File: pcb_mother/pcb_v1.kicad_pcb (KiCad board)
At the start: 2 copper layers, 90.1 x 71.5 mm, 37 parts, among them J1 Conn_01x02, J10 Conn_01x02, J11 Conn_01x06, J12 Conn_01x02, J13 Conn_01x02, J14 Conn_01x06, J3 Conn_01x02, J4 Conn_01x02_Male, J5 Conn_01x02_Male, J6 Conn_01x02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

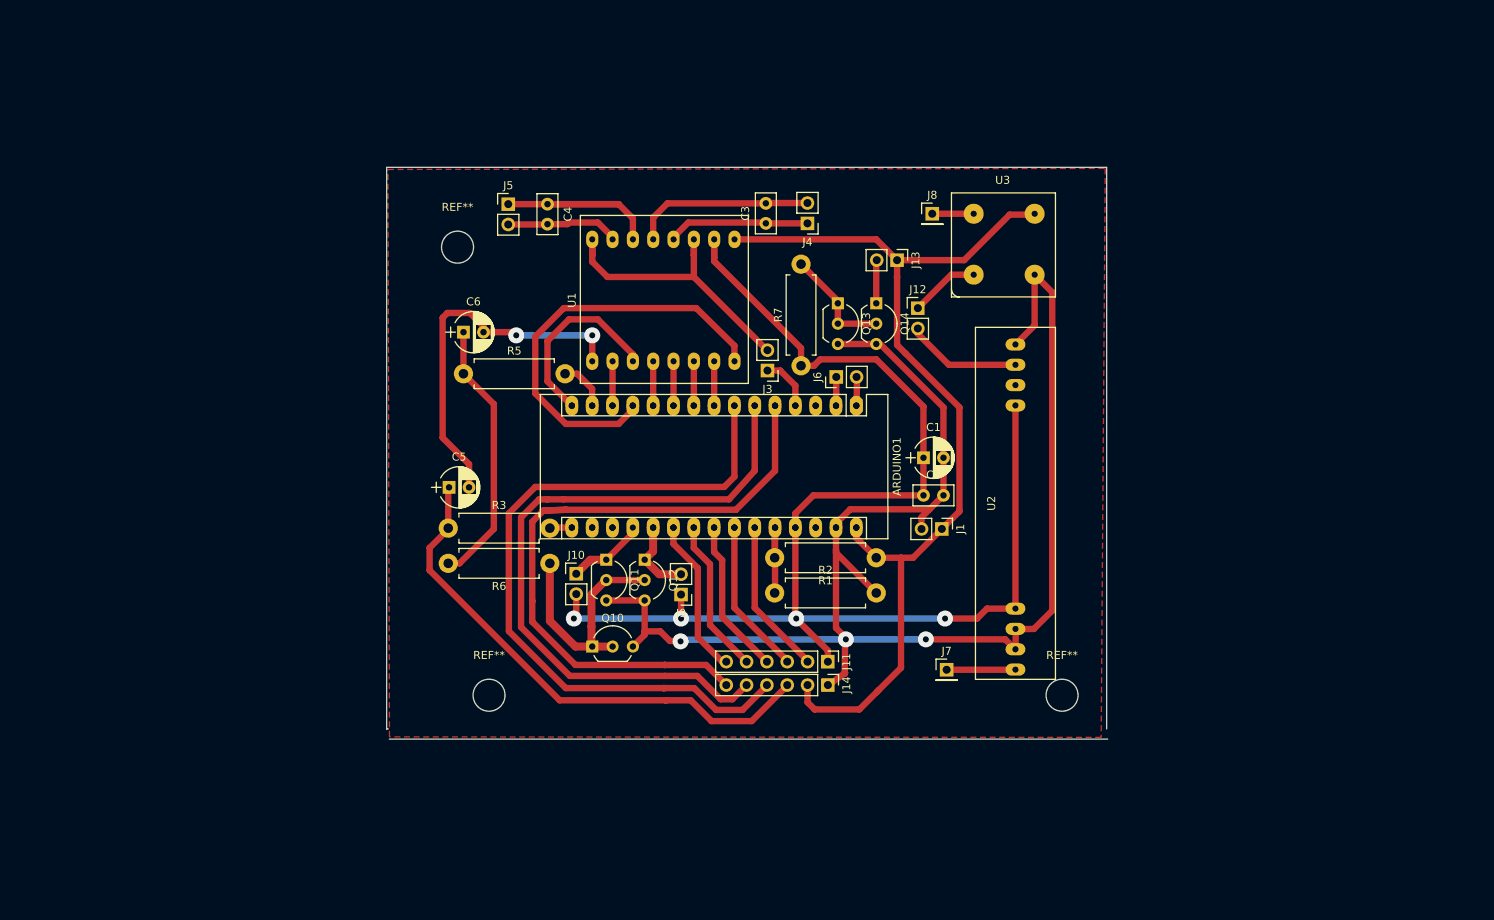
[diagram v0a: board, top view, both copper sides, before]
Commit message: Se moifico el esquematico y se esta acomodando para poder armar el pcb, la linea que se va a seguir es priorizar el funcionamiento antes que la estetica y el espacio.
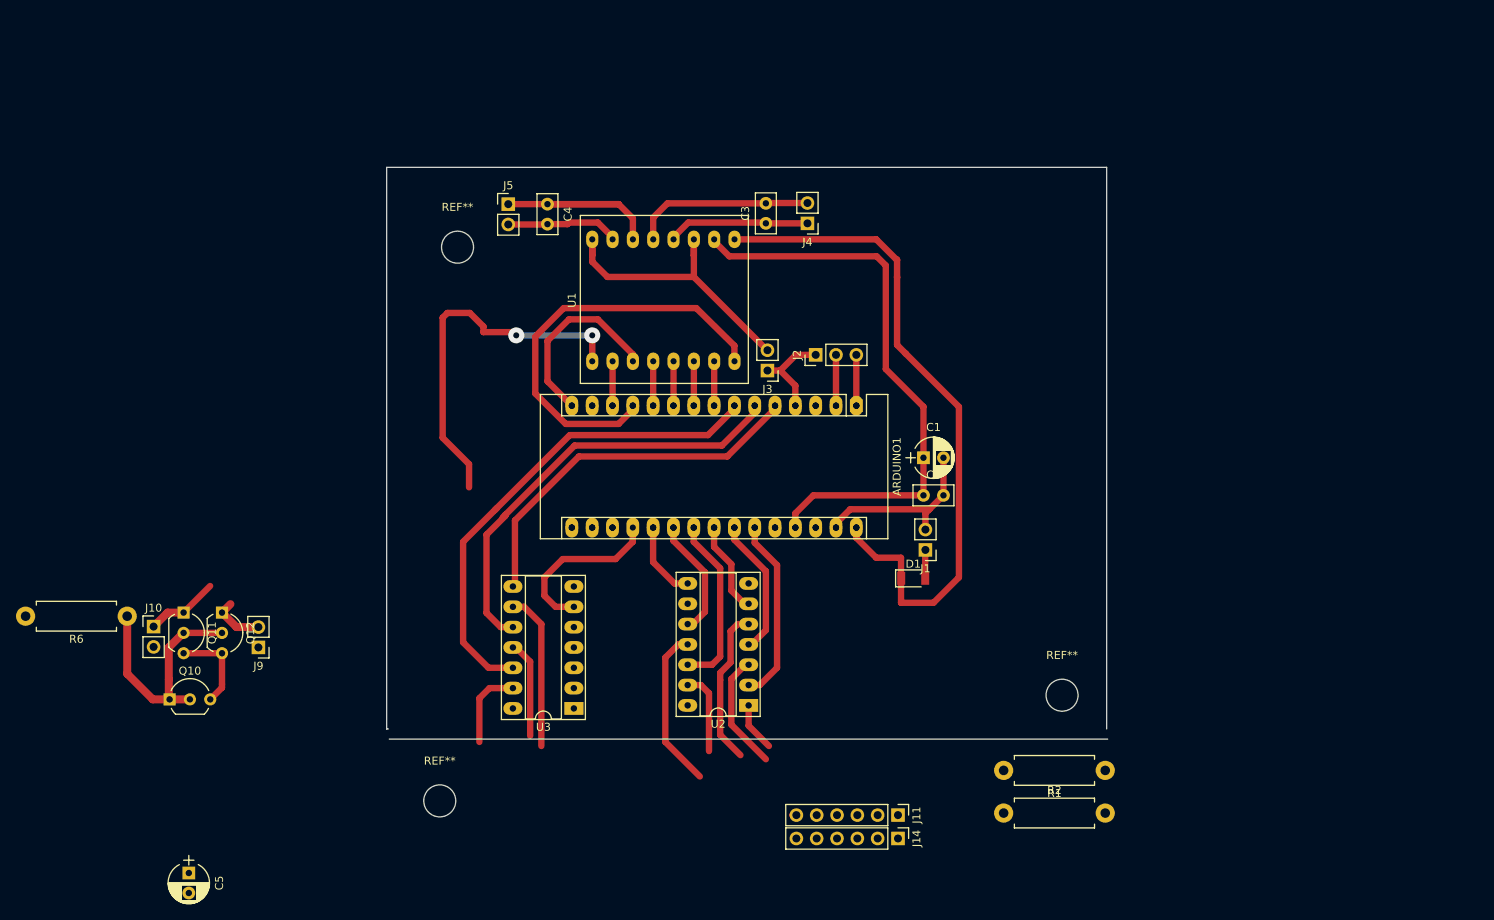
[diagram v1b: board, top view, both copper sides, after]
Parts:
- removed C6: 2.2u, Capacitors_THT:CP_Radial_D5.0mm_P2.50mm
- removed J12, J13, J6: Conn_01x02, Pin_Headers:Pin_Header_Straight_1x02_Pitch2.54mm
- removed J7, J8: Conn_01x01, Pin_Headers:Pin_Header_Straight_1x01_Pitch2.54mm
- removed Q13, Q14: 2N2219, TO_SOT_Packages_THT:TO-92_Inline_Wide
- removed R3, R5: 100k, Resistors_THT:R_Axial_DIN0411_L9.9mm_D3.6mm_P12.70mm_Horizontal
- removed R7: 220, Resistors_THT:R_Axial_DIN0411_L9.9mm_D3.6mm_P12.70mm_Horizontal
- added D1: D, Diodes_SMD:D_1206, F.Cu at (134.6, 103.4)
- added J2: Conn_01x03, Pin_Headers:Pin_Header_Straight_1x03_Pitch2.54mm, F.Cu at (122.4, 75.4)
- U2: value Rws433mhz -> 74HCT04; footprint Propias:rws433 -> Housings_DIP:DIP-14_W7.62mm_Socket_LongPads
- U3: value tws -> 74HCT04; footprint Propias:tws433 -> Housings_DIP:DIP-14_W7.62mm_Socket_LongPads
- moved U3 79.6 mm to (92.2, 119.6)
- moved C5 58.2 mm to (44.1, 140.2), turned to 270 degrees
- moved J10 53.2 mm to (39.7, 109.4)
- moved Q10 53.2 mm to (41.7, 118.5)
- moved Q11 53.2 mm to (43.4, 107.7)
- moved R6 53.2 mm to (36.4, 108.1)
- moved J9 53.2 mm to (52.8, 112.0)
- moved Q12 53.2 mm to (48.2, 107.7)
- moved U2 41.2 mm to (114.0, 119.3), turned to 180 degrees
- moved R2 39.7 mm to (145.9, 132.7)
- moved R1 39.1 mm to (158.6, 127.4)
- moved J11 21.1 mm to (132.7, 133.0)
- moved J14 21.1 mm to (132.7, 135.9)
- moved REF** 14.6 mm to (75.4, 131.2)
- moved J1 3.33 mm to (136.1, 99.8), turned to 180 degrees
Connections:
- ARDUINO1 pad 14: /Encoders -> Net-(ARDUINO1-Pad14)
- ARDUINO1 pad 16: /S_linea -> Net-(ARDUINO1-Pad16)
- ARDUINO1 pad 19: /E1 -> /A0_E1
- ARDUINO1 pad 20: /E2 -> /A1_E2
- ARDUINO1 pad 21: /L1_a -> /A2_l1_A
- ARDUINO1 pad 22: /L2_a -> /A3_l2_A
- ARDUINO1 pad 23: /L3_a -> /A4_l3_A
- ARDUINO1 pad 24: /L4_a -> /A5_l4_A
- ARDUINO1 pad 25: /L5_a -> /A6_l5_A
- ARDUINO1 pad 5: /L8_a -> /D2_L8_a
- ARDUINO1 pad 6: /L7_a -> /D3_L7_a
- ARDUINO1 pad 7: /L6_a -> /D4_L6_a
- C1 pad 1: /Vcc_5v -> Net-(C1-Pad1)
- J1 pad 1: /Vcc_bat -> Net-(D1-Pad2)
- R6 pad 2: Net-(C6-Pad1) -> /Vcc_5v
- U2 pad 1: /gnd_logic -> /L5_a
- U2 pad 2: /Comunicacion_RX -> /A6_l5_A
- U2 pad 3: Net-(U2-Pad3) -> /L4_a
- U2 pad 4: /Vcc_5v -> /A5_l4_A
- U2 pad 5: Net-(J7-Pad1) -> /L3_a
- U3 pad 1: /Comunicacion_TX -> (no net)
- U3 pad 2: /Vcc_bat -> (no net)
- U3 pad 3: /gnd_logic -> (no net)
- U3 pad 4: Net-(J8-Pad1) -> (no net)
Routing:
- net /gnd_logic: track 249.2 -> 93.4 mm, vias 5 -> 2
- net /Vcc_5v: track 175.8 -> 61.5 mm, vias 4 -> 0
- net /L6_a: track 91.8 -> 10.4 mm
- net /L7_a: track 86.4 -> 12.2 mm
- net /S_lin_ref_a: track 66.2 -> 0.06 mm
- net /L8_a: track 84.4 -> 19.8 mm
- net /D4_L6_a: track 0.00 -> 61.7 mm
- net /D3_L7_a: track 0.00 -> 55.1 mm
- net /D2_L8_a: track 0.00 -> 47.0 mm
- net /Vcc_bat: track 123.7 -> 86.8 mm
- net Net-(C6-Pad1): track 33.7 -> 0.00 mm
- net /A6_l5_A: track 0.00 -> 23.1 mm
- net /A0_E1: track 0.00 -> 23.1 mm
- net /A3_l2_A: track 0.00 -> 22.0 mm
- net /A5_l4_A: track 0.00 -> 17.5 mm
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- removed copper zone on F.Cu, net /gnd_logic

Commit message: modificacion del pcb previas a hacer una nueva rama.
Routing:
- net /E2: track 6.80 -> 30.5 mm

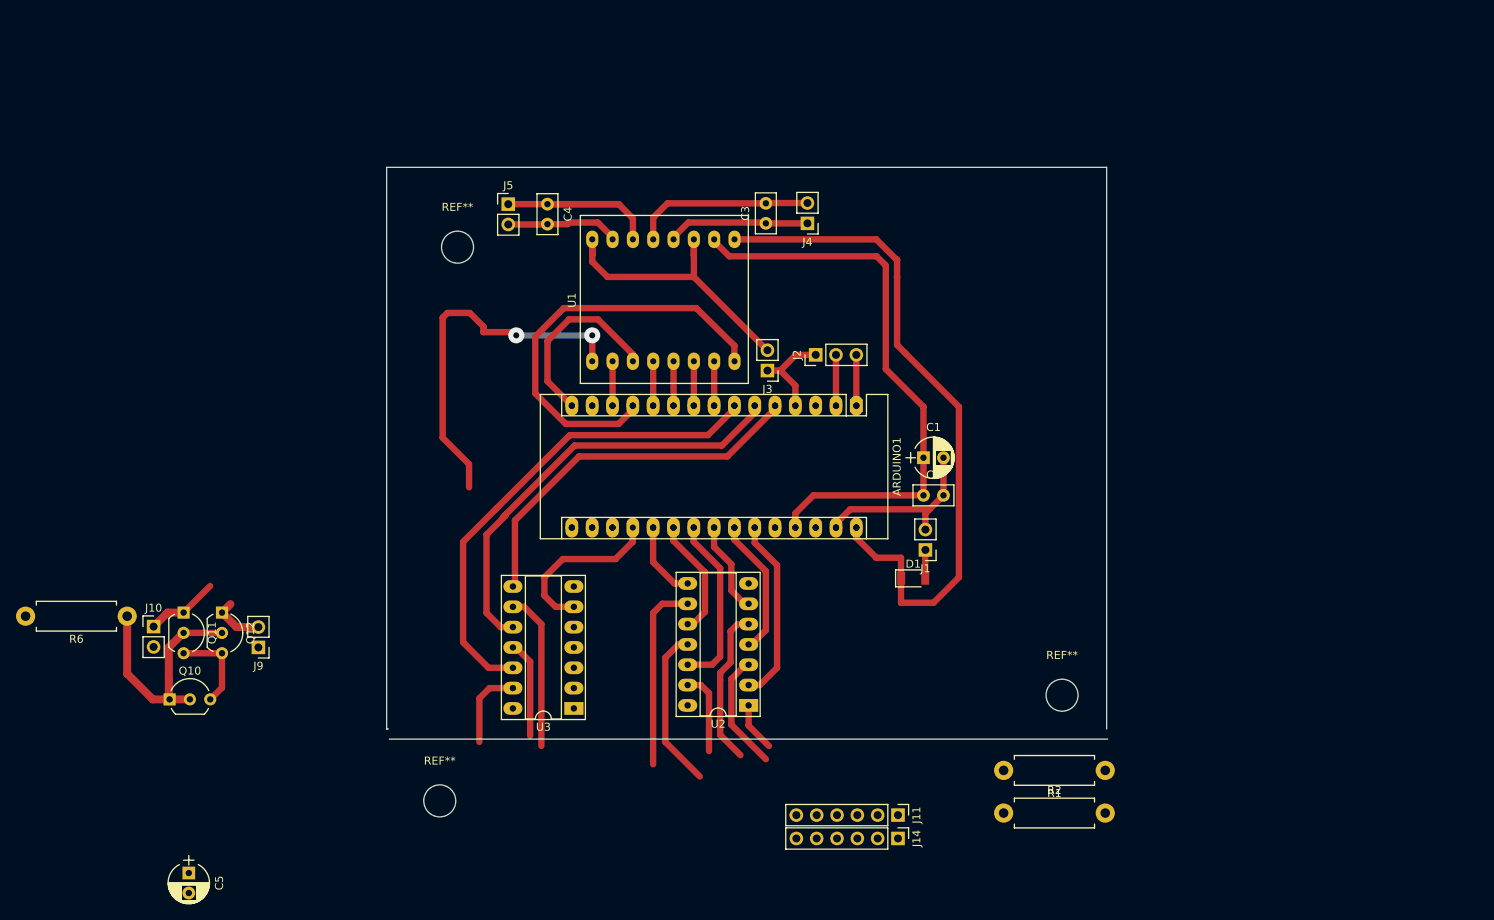
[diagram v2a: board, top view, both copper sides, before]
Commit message: Se pudiron acomodar los inversores, ahora falta poner el divisor resistivo, los planos de tierra, los puentes y los aujeros...
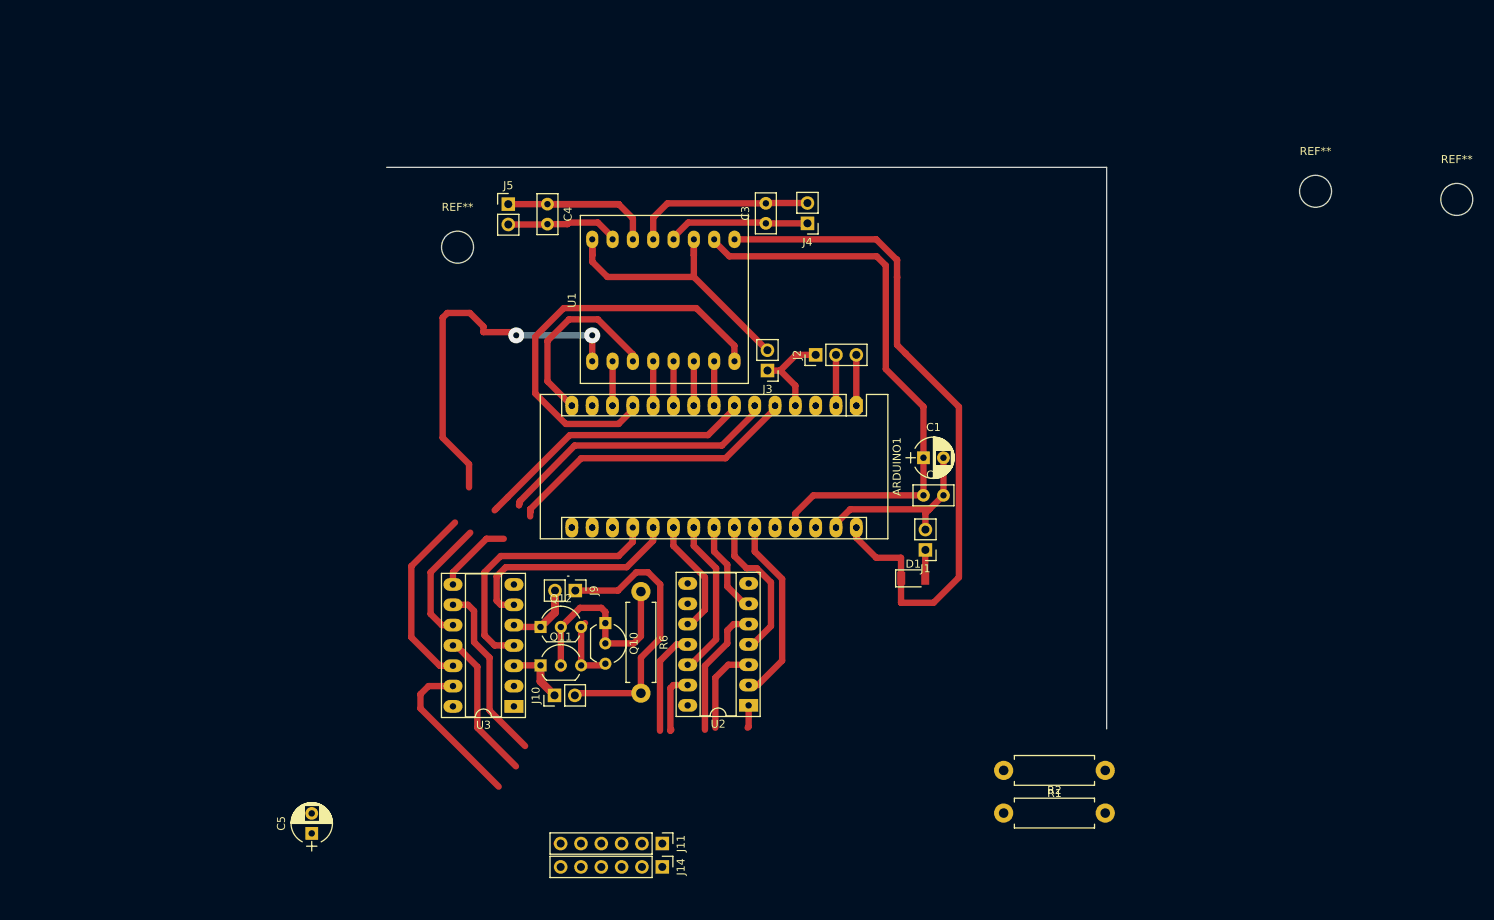
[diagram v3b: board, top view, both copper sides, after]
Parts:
- moved REF** 133.4 mm to (184.9, 55.0)
- moved REF** 79.2 mm to (202.6, 56.0)
- moved R6 64.3 mm to (100.6, 105.0), turned to 270 degrees
- moved Q10 55.3 mm to (96.1, 109.0), turned to 270 degrees
- moved J10 50.8 mm to (89.8, 118.0), turned to 90 degrees
- moved Q11 45.1 mm to (88.0, 114.3), turned to 0 degrees
- moved J9 40.2 mm to (92.4, 104.9), turned to 270 degrees
- moved Q12 39.9 mm to (88.0, 109.5), turned to 0 degrees
- moved J11 29.7 mm to (103.3, 136.5)
- moved J14 29.7 mm to (103.3, 139.4)
- moved C5 16.1 mm to (59.4, 135.3), turned to 90 degrees
- moved U3 7.50 mm to (84.7, 119.4)
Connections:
- ARDUINO1 pad 27: /Vcc_5v -> VCC
- C2 pad 1: /Vcc_5v -> VCC
- J10 pad 1: /E1 -> /E2
- J10 pad 2: /Vcc_5v -> VCC
- J11 pad 1: /Vcc_5v -> VCC
- J9 pad 1: /Vcc_5v -> VCC
- J9 pad 2: /E2 -> /E1
- Q11 pad 1: /E1 -> /E2
- Q12 pad 1: /E2 -> /E1
- R6 pad 2: /Vcc_5v -> VCC
- U1 pad 2: /Vcc_5v -> VCC
- U2 pad 8: /A1_E2 -> (no net)
- U2 pad 9: /E2 -> (no net)
- U3 pad 3: (no net) -> /E2
- U3 pad 4: (no net) -> /A0_E1
- U3 pad 6: /A0_E1 -> /A1_E2
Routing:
- net /Vcc_5v: track 61.5 -> 0.00 mm
- net VCC: track 0.00 -> 57.0 mm
- net Net-(C1-Pad1): track 11.1 -> 50.7 mm
- net /E2: track 30.5 -> 8.17 mm
- net /A1_E2: track 11.0 -> 29.7 mm
- net /A0_E1: track 23.1 -> 37.1 mm
- net /L6_a: track 10.4 -> 20.4 mm
- net /L7_a: track 12.2 -> 18.6 mm
- net /L1_a: track 20.6 -> 14.7 mm
- net /Vref_encoders: track 30.5 -> 26.9 mm
- net /D3_L7_a: track 55.1 -> 51.5 mm
- net /L5_a: track 6.26 -> 2.97 mm
- net /L4_a: track 14.8 -> 11.6 mm
- net /L3_a: track 19.7 -> 16.6 mm
- net /L8_a: track 19.8 -> 22.6 mm
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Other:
- board size 90.1 x 71.5 mm -> 90 x 70.2 mm

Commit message: Casi termino la placa, falta el plano de tierra, algunos puentes y los aujeros de montaje.
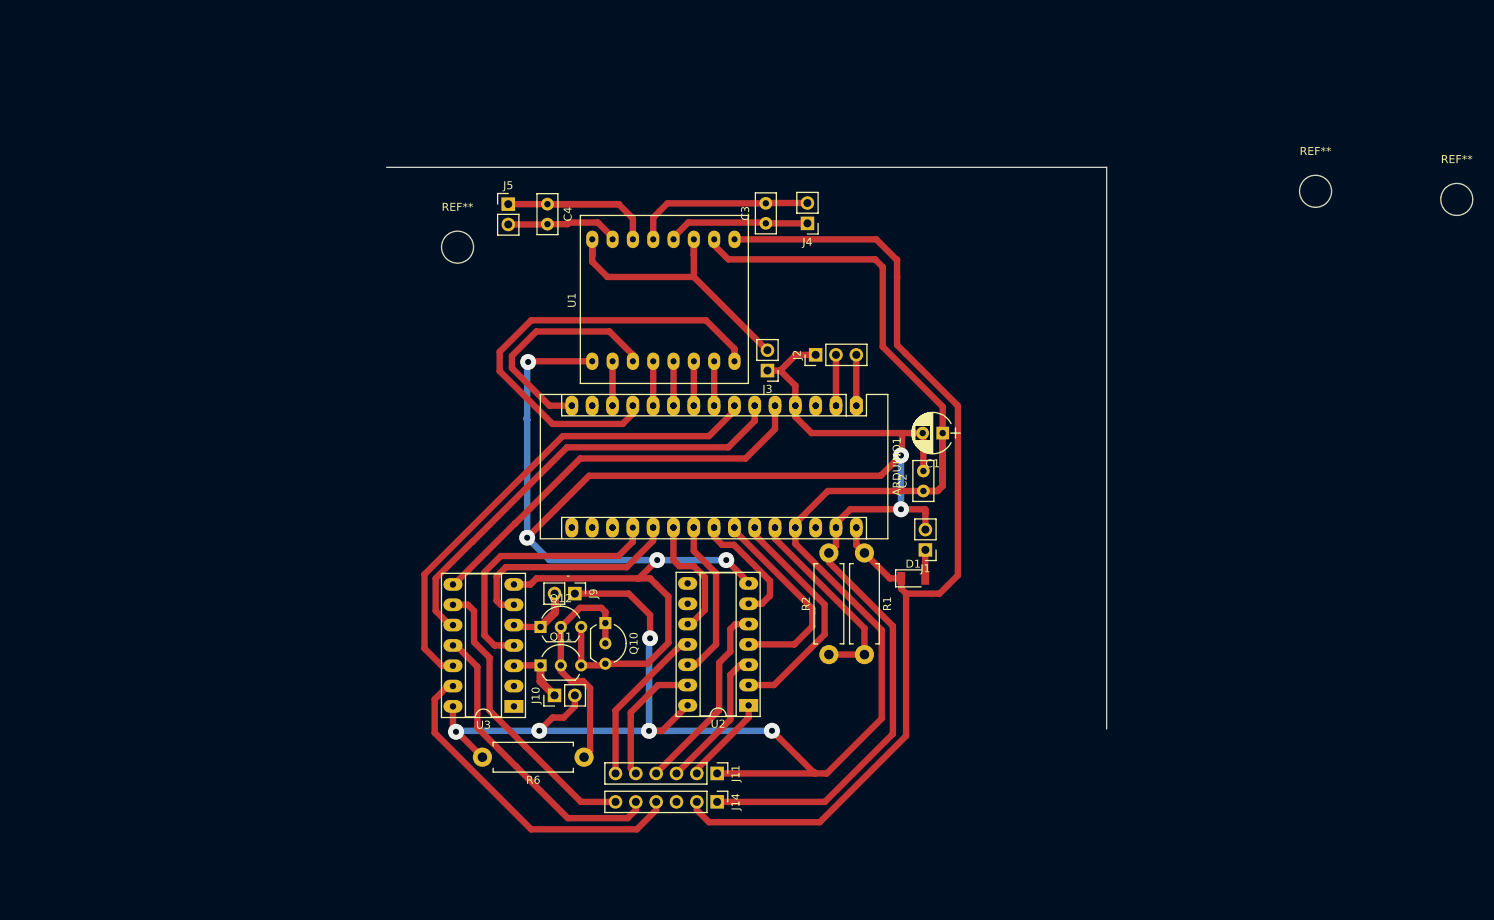
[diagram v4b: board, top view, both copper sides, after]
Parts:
- removed C5: 2.2u, Capacitors_THT:CP_Radial_D5.0mm_P2.50mm
- C1: value CP -> 10u
- moved R1 40.6 mm to (128.5, 100.2), turned to 270 degrees
- moved R2 29.5 mm to (124.1, 112.9), turned to 90 degrees
- moved R6 21.9 mm to (93.5, 125.7), turned to 180 degrees
- moved J11 11.1 mm to (110.1, 127.8)
- moved J14 10.6 mm to (110.1, 131.3)
- moved C1 3.91 mm to (138.3, 85.2), turned to 180 degrees
- moved C2 0.54 mm to (135.9, 92.5), turned to 90 degrees
- moved J9 0.38 mm to (92.3, 105.3)
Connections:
- ARDUINO1 pad 29: /gnd_logic -> GND
- ARDUINO1 pad 4: /gnd_logic -> GND
- C1 pad 1: Net-(C1-Pad1) -> VCC
- C1 pad 2: /gnd_logic -> GND
- C2 pad 2: /gnd_logic -> GND
- J1 pad 2: /gnd_logic -> GND
- J14 pad 1: /gnd_logic -> GND
- J14 pad 3: /S_lin_ref_a -> Net-(J14-Pad3)
- J2 pad 1: /gnd_logic -> GND
- J3 pad 1: /gnd_logic -> GND
- Q10 pad 3: /gnd_logic -> GND
- Q11 pad 3: /gnd_logic -> GND
- Q12 pad 3: /gnd_logic -> GND
- R2 pad 2: /gnd_logic -> GND
- U1 pad 9: /gnd_logic -> GND
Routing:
- net GND: track 0.00 -> 273.4 mm, vias 0 -> 6
- net VCC: track 57.0 -> 230.5 mm, vias 0 -> 5
- net /gnd_logic: track 90.9 -> 0.00 mm, vias 2 -> 0
- net Net-(C1-Pad1): track 50.7 -> 0.00 mm
- net /Vcc_bat: track 86.8 -> 135.0 mm
- net /Nivel_bat: track 0.07 -> 25.0 mm
- net /L6_a: track 20.4 -> 41.9 mm
- net /L7_a: track 18.6 -> 37.7 mm
- net /L8_a: track 22.6 -> 36.7 mm
- net /L2_a: track 7.83 -> 16.8 mm
- net /L5_a: track 2.97 -> 11.2 mm
- net /L3_a: track 16.6 -> 24.4 mm
- net /A5_l4_A: track 19.2 -> 26.4 mm
- net /L1_a: track 14.7 -> 21.6 mm
- net /A6_l5_A: track 23.5 -> 30.2 mm
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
